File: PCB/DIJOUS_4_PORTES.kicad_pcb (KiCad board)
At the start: 2 copper layers, 96.9 x 106.2 mm, 67 parts, among them J1 PowerIN, J10 DOOR_LCK, J12 WIN_SW, J14 FINAL_CARRERA_UP, J15 FINAL_CARRERA_DOWN, J2 OUT_WIN, J3 ICSP, J4 CAN, J5 OUT_DOOR, J6 USART, J7 SPI, J8 RFID_COAX, SW1 DOOR_LCK, SW3 WIN_SW, U1 LT1528CT-PBF, U2 PIC32MK0256MCJ048-I/Y8X, U3 TCAN334D, U4 MAX22201ATC+, U5 MAX22201ATC+, Y1 ASZKDV-32.768KHZ-L-T3, Y2 ECS-3225SMV-080-GP-TR

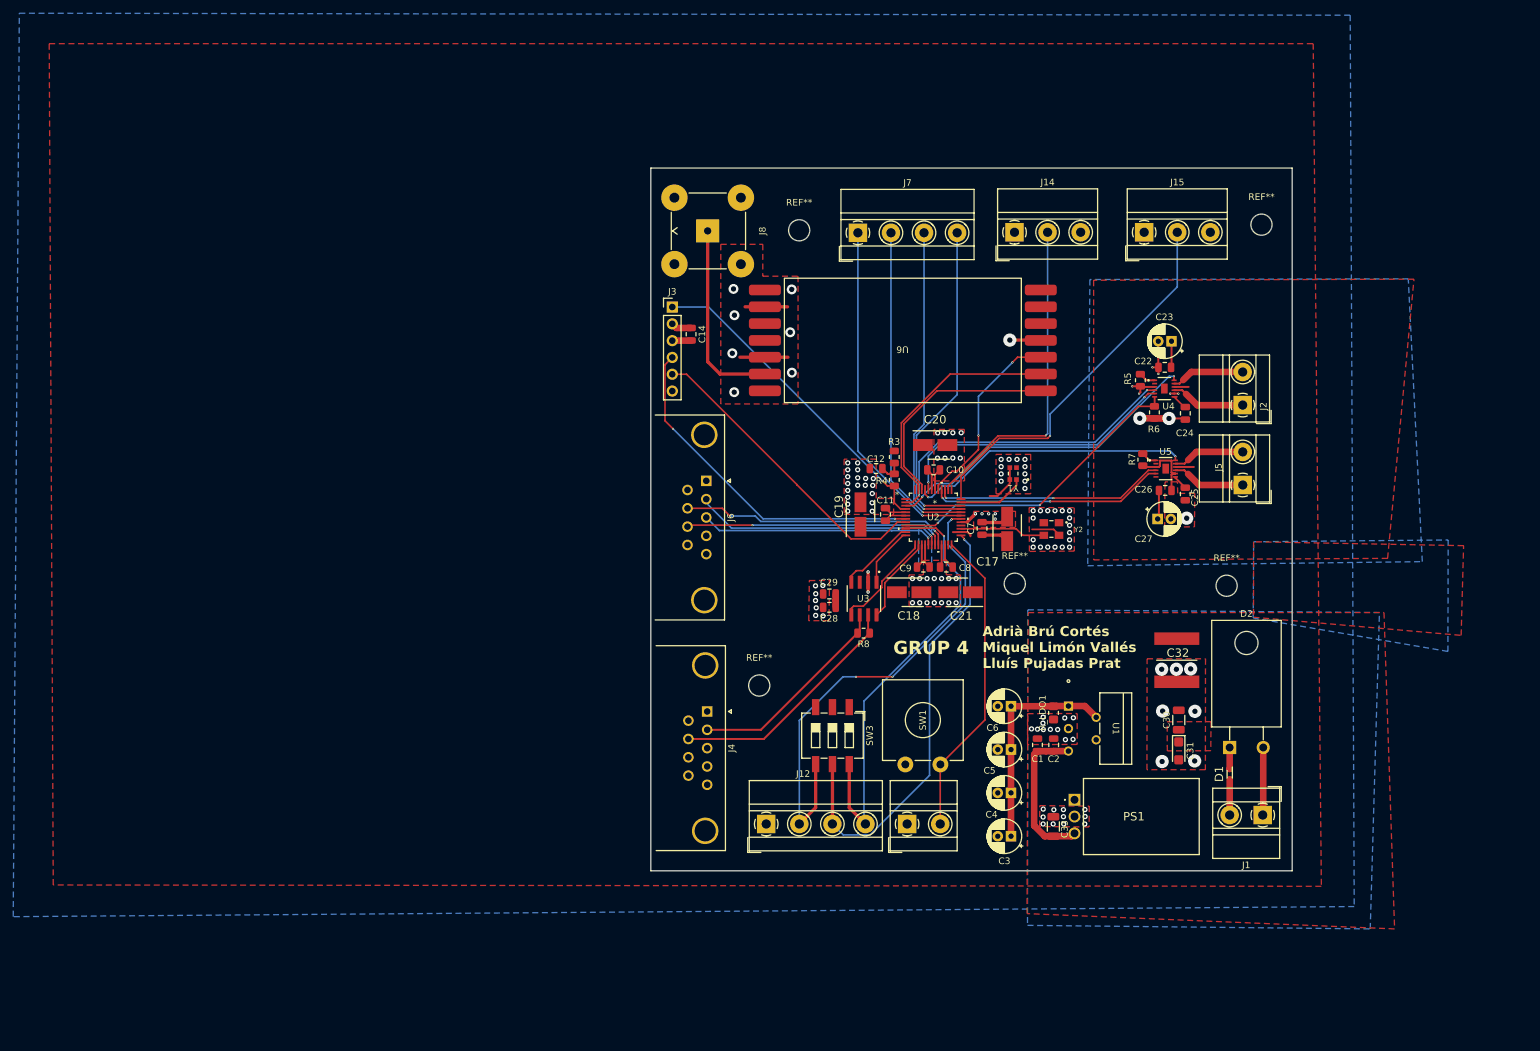
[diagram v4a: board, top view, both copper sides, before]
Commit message: PCB LAYOUT 2.0 - rearranged uc pins, changed smd Cs to ceramic
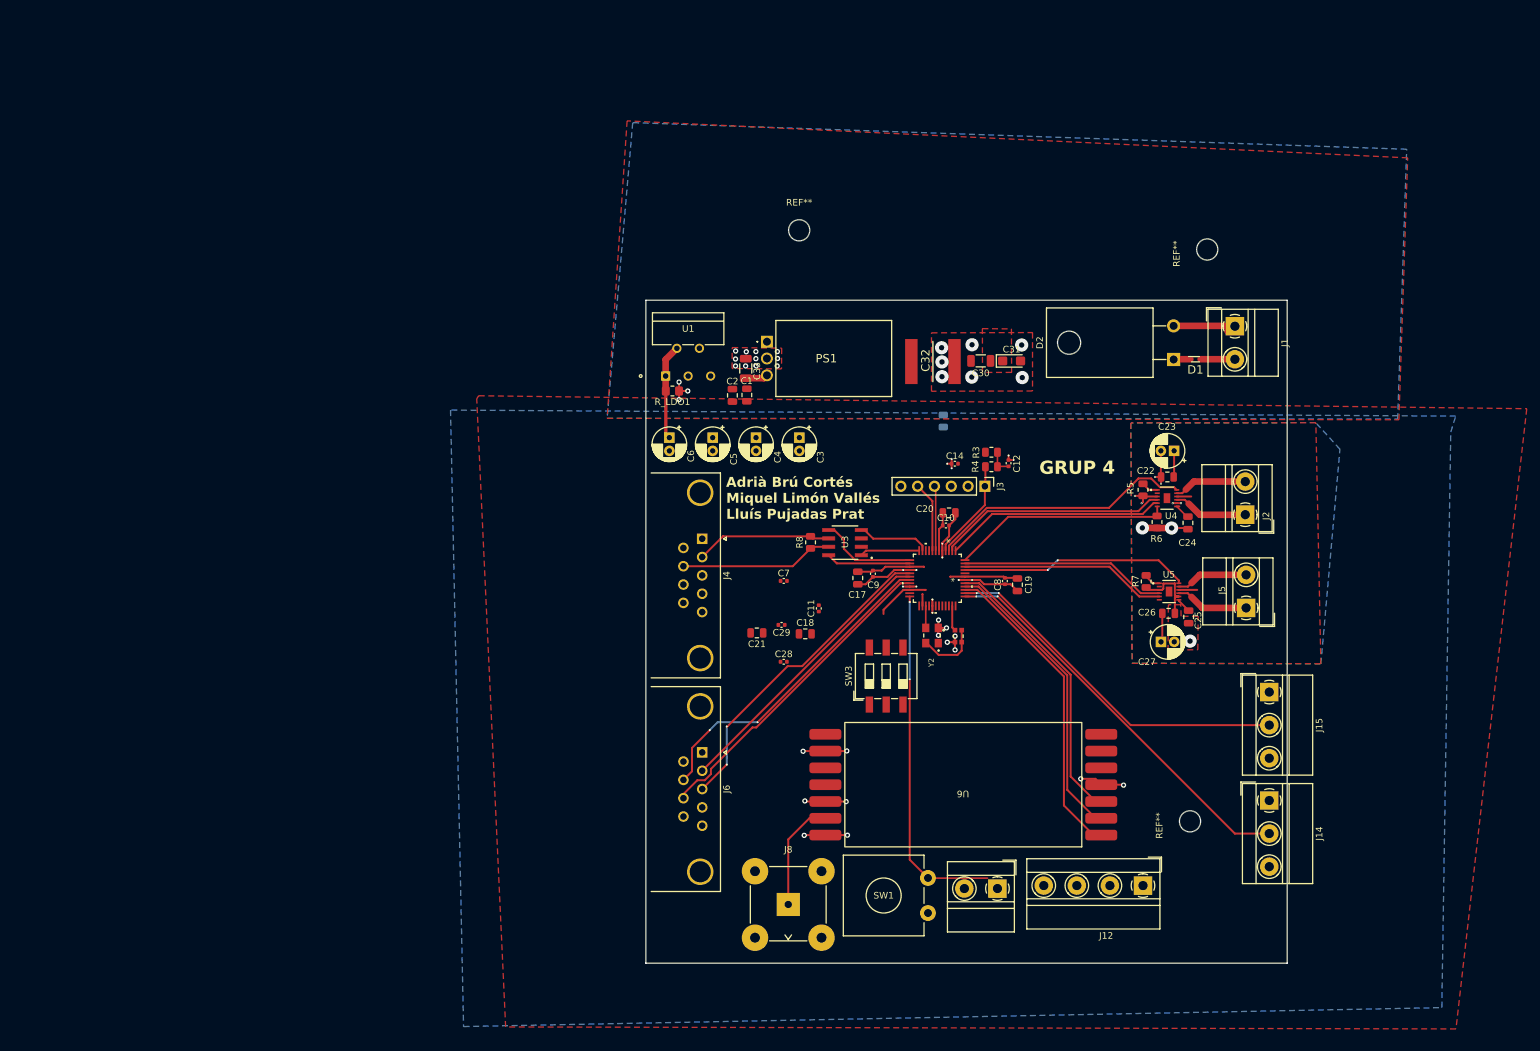
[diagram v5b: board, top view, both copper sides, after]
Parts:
- removed J7: SPI, TerminalBlock_MetzConnect:TerminalBlock_MetzConnect_Type011_RT05504HBWC_1x04_P5.00mm_Horizontal
- removed the REF** at (160.0, 132.0)
- removed the REF** at (235.9, 62.3)
- removed the REF** at (230.6, 116.9)
- added R1: 0, Resistor_SMD:R_0805_2012Metric, B.Cu at (187.8, 92.0)
- added REF**: MountingHole_3.2mm_M3, MountingHole:MountingHole_3.2mm_M3, F.Cu at (225.1, 152.5)
- C10, C11, C12, C14, C28, C29, C7, C8, C9: footprint Capacitor_SMD:C_0805_2012Metric -> Capacitor_SMD:C_0402_1005Metric
- C17, C18, C19, C20, C21: footprint kicad_models:CAPAE430X550N -> Capacitor_SMD:C_0805_2012Metric
- moved J8 102.5 mm to (164.4, 165.1), turned to 180 degrees
- moved J14 94.1 mm to (237.1, 149.3), turned to -90 degrees
- moved C33 83.4 mm to (158.0, 84.0)
- moved PS1 83.4 mm to (161.2, 80.0)
- moved U1 78.7 mm to (145.8, 85.2), turned to 0 degrees
- moved R_LDO1 75.4 mm to (146.9, 87.5), turned to 180 degrees
- moved J1 74.0 mm to (231.9, 77.7), turned to -90 degrees
- moved J15 72.0 mm to (237.1, 133.0), turned to -90 degrees
- moved C2 71.8 mm to (155.9, 88.1), turned to -90 degrees
- moved C1 68.8 mm to (158.1, 88.1), turned to -90 degrees
- moved C3 68.2 mm to (166.1, 94.5), turned to -90 degrees
- moved U6 67.8 mm to (190.8, 147.8)
- moved C4 66.1 mm to (159.5, 94.5), turned to -90 degrees
- moved C6 65.7 mm to (146.4, 94.5), turned to -90 degrees
- moved C5 65.2 mm to (153.0, 94.5), turned to -90 degrees
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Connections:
- net CANH renamed CAN_P
- net CANL renamed CAN_N
- U2 pad 1: unconnected-(U2-TCK/RPA7/PWM4L/RA7-Pad1) -> WIN_IN2
- U2 pad 10: WIN_SW3 -> unconnected-(U2-OA2IN+/AN1/C2IN1+/RPA1/RA1-Pad10)
- U2 pad 19: /UART_CTS -> UART_CLK
- U2 pad 20: UART_CLK -> /UART_CTS
- U2 pad 23: unconnected-(U2-TDI/DAC2/AN26/CVD26/RPA8/SDA2/RA8-Pad23) -> WIN_SW3
- U2 pad 31: SPI_SS -> unconnected-(U2-PGD2/RPB5/SDA1/RB5-Pad31)
- U2 pad 32: SPI_SDO -> unconnected-(U2-PGC2/RPB6/SCL1/RB6-Pad32)
- U2 pad 33: SPI_SDI -> unconnected-(U2-DAC1/AN48/CVD48/RPC10/RC10-Pad33)
- U2 pad 34: SPI_CK -> unconnected-(U2-OA5OUT/AN25/CVD25/C5IN4-/RPB7/SCK1/INT0/RB7-Pad34)
- U2 pad 36: FINAL_CARRERA_DOWN -> unconnected-(U2-SOSCO/RPB8/T1CK/RB8-Pad36)
- U2 pad 37: unconnected-(U2-TMS/OA5IN-/AN27/CVD27/LVDIN/C5IN1-/RPB9/RB9-Pad37) -> FINAL_CARRERA_UP
- U2 pad 38: FINAL_CARRERA_UP -> FINAL_CARRERA_DOWN
- U2 pad 39: DOOR_IN1 -> RFID_IN
- U2 pad 40: DOOR_IN2 -> RFID_OUT
- U2 pad 44: WIN_IN2 -> unconnected-(U2-RPB10/PWM3H/RB10-Pad44)
- U2 pad 46: RFID_IN -> DOOR_IN2
- U2 pad 47: RFID_OUT -> DOOR_IN1
- U2 pad 48: unconnected-(U2-TDO/PWM4H/RA10-Pad48) -> ISEN_WIN
- U2 pad 9: ISEN_WIN -> unconnected-(U2-OA2OUT/AN0/C2IN4-/C4IN3-/RPA0/RA0-Pad9)
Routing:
- net WIN_SW1: track 73.6 -> 0.00 mm, vias 3 -> 0
- net WIN_SW3: track 67.6 -> 0.00 mm, vias 1 -> 0
- net WIN_SW2: track 67.5 -> 0.00 mm, vias 1 -> 0
- net SPI_SS: track 52.6 -> 0.00 mm, vias 1 -> 0
- net SPI_SDO: track 50.0 -> 0.00 mm, vias 1 -> 0
- net SPI_CK: track 49.8 -> 0.00 mm, vias 1 -> 0
- net SPI_SDI: track 48.6 -> 0.00 mm, vias 1 -> 0
- net PGEDx: track 52.6 -> 9.81 mm, vias 2 -> 0
- net PGECx: track 46.7 -> 10.7 mm
- net /MCLR: track 49.5 -> 15.2 mm, vias 1 -> 0
- net GND: track 45.1 -> 67.6 mm, vias 92 -> 29
- net +5V: track 23.6 -> 3.72 mm
- net RFID_RST: track 28.9 -> 43.3 mm, vias 2 -> 0
- net CAN_P: track 36.9 -> 23.2 mm
- net RFID_IN: track 33.8 -> 47.4 mm
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- removed copper zone on F.Cu, net GND
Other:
- board size 96.9 x 106.2 mm -> 96.9 x 100.2 mm

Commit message: arreglos
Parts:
- C10, C11, C17, C18, C19, C20, C21, C7, C8, C9: moved to B.Cu
- moved REF** 129.0 mm to (147.9, 167.3)
- moved C30 30.3 mm to (223.5, 87.2)
- moved C31 30.3 mm to (228.1, 87.3)
- moved C32 30.3 mm to (216.2, 87.3)
- moved C33 29.7 mm to (187.0, 77.7), turned to -90 degrees
- moved C7 29.4 mm to (193.1, 115.5), turned to -90 degrees
- moved C28 24.4 mm to (173.9, 106.2), turned to -90 degrees
- moved PS1 22.7 mm to (183.8, 81.7), turned to 180 degrees
- moved REF** 21.6 mm to (147.7, 74.6)
- moved C21 21.1 mm to (178.2, 114.1), turned to 90 degrees
- moved C17 19.9 mm to (194.8, 115.3)
- moved C29 19.0 mm to (172.8, 106.2), turned to 90 degrees
- moved C8 16.5 mm to (180.7, 116.8)
- moved C11 16.4 mm to (185.2, 117.6), turned to 0 degrees
- moved REF** 14.1 mm to (228.2, 166.3)
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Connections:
- SW3 pad 4: WIN_SW1 -> WIN_SW3
- SW3 pad 6: WIN_SW3 -> WIN_SW1
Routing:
- net WIN_SW1: track 0.00 -> 64.4 mm, vias 0 -> 2
- net WIN_SW3: track 0.00 -> 61.0 mm
- net WIN_SW2: track 0.00 -> 60.2 mm
- net +5V: track 3.72 -> 36.0 mm
- net GND: track 67.6 -> 42.6 mm, vias 29 -> 63
- net FINAL_CARRERA_DOWN: track 54.3 -> 43.8 mm
- net GNDPWR: track 39.1 -> 29.1 mm, vias 30 -> 37
- net /FAULT_DOOR: track 34.6 -> 26.5 mm
- net WIN_IN2: track 33.5 -> 26.1 mm
- net WIN_IN1: track 34.5 -> 27.3 mm
- net /FAULT_WIN: track 40.1 -> 33.4 mm
- net ISEN_WIN: track 33.2 -> 26.9 mm
- net DOOR_IN1: track 31.2 -> 25.0 mm
- net DOOR_IN2: track 31.2 -> 25.1 mm
- net /DIGITAL/clk2i: track 3.84 -> 7.90 mm
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- added copper zone on B.Cu, net +3.3V
- added copper zone on F.Cu, net GND
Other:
- board size 96.9 x 100.2 mm -> 91.2 x 101.1 mm
